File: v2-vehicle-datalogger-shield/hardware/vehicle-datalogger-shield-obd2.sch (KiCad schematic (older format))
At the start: 47 parts

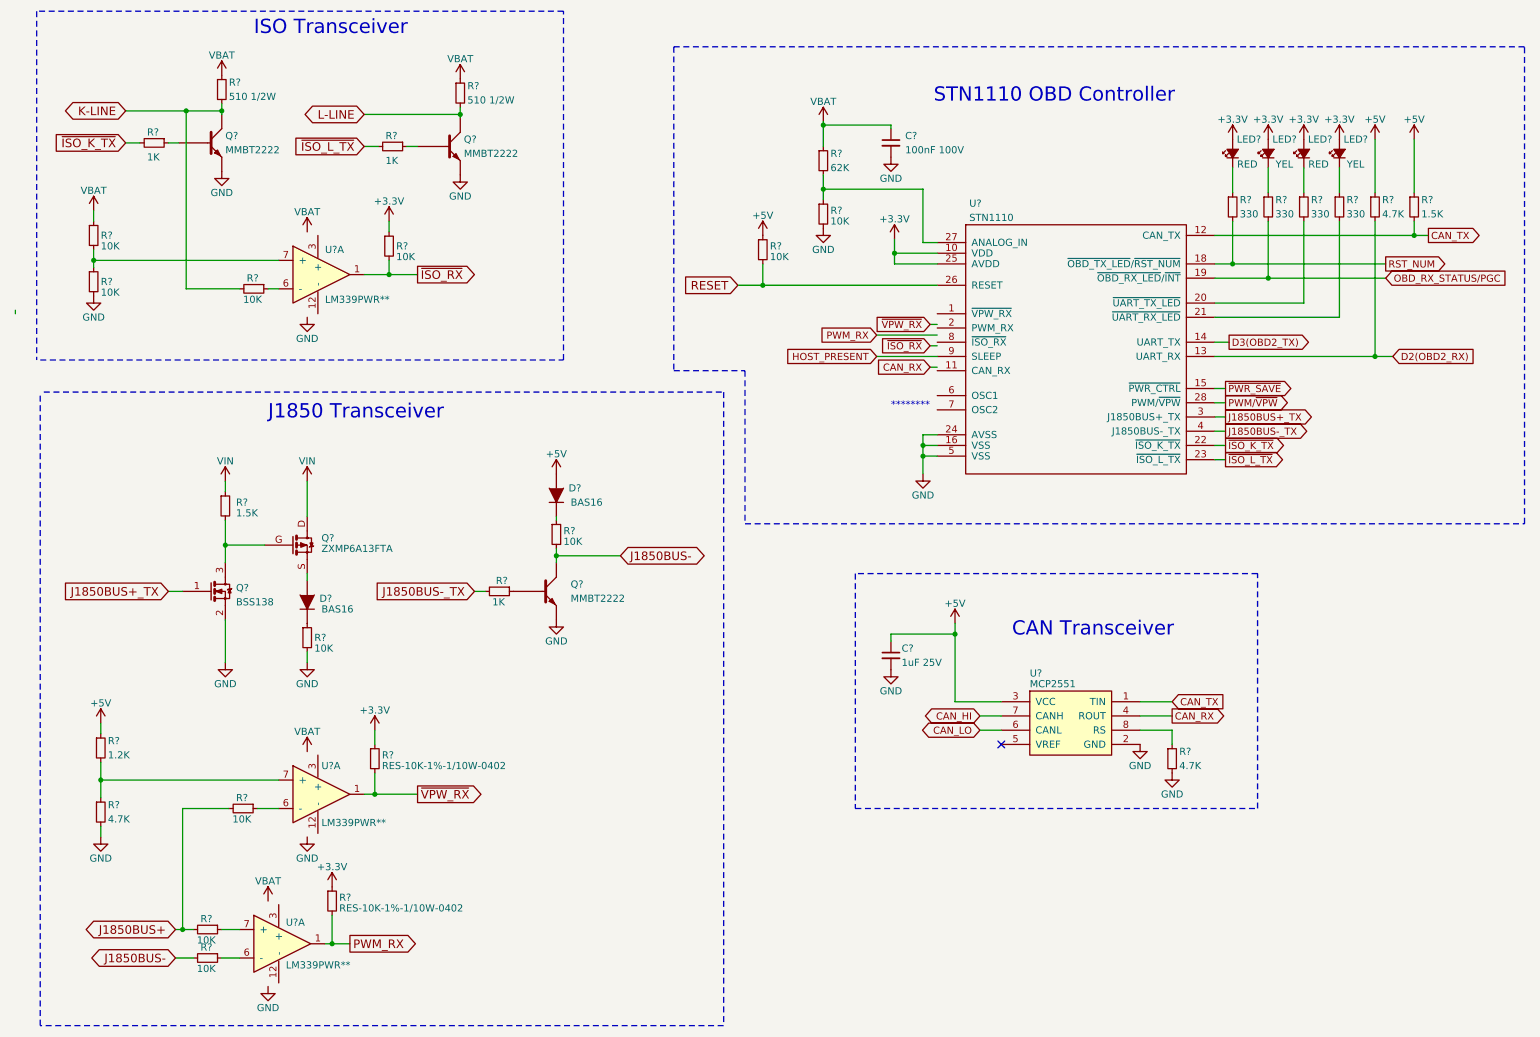
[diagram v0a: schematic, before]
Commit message: Added CC3000 and fixed all other packages. Ready for check.
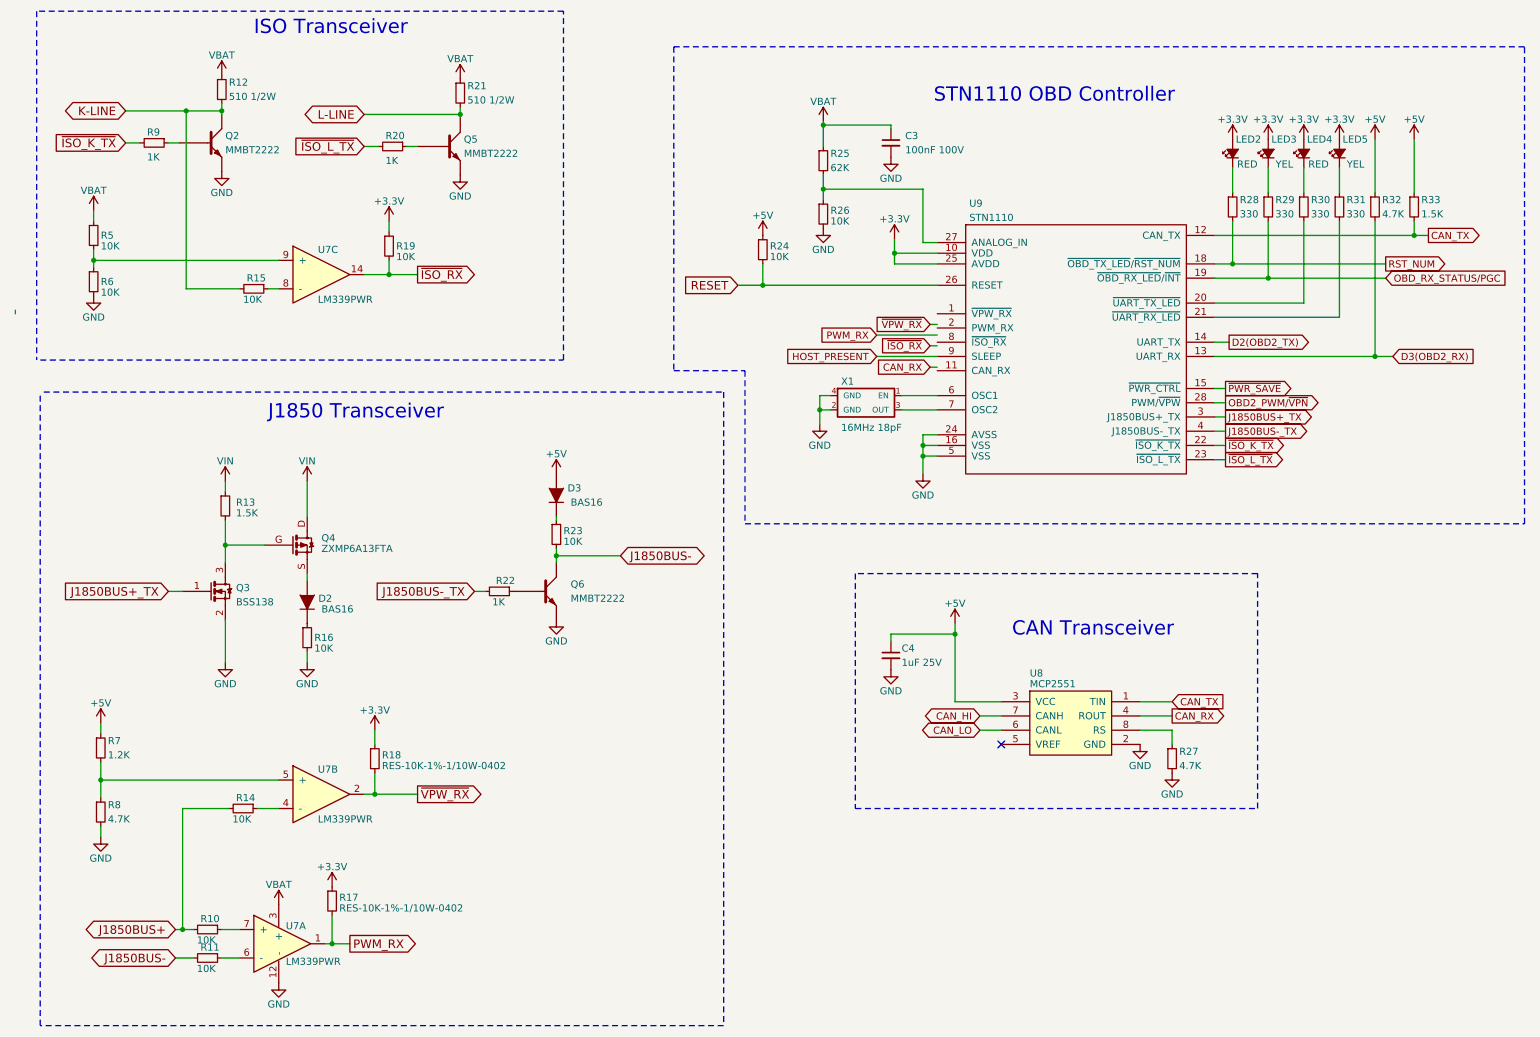
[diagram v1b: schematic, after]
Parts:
- removed U? (x3): LM339PWR**, TSSOP14, symbol IC-DIFF-COMPARE-LM339PWR-TSSOP14
- added U7: LM339PWR, TSSOP14, symbol IC-DIFF-COMPARE-LM339PWR-TSSOP14
- added X1: 16MHz 18pF, CTS-4SMD, symbol CRYSTAL-16MHZ-18PF-40OHM-CTS-4SMD
- gave numbers to parts that had none: 44
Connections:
- net labels added: D2(OBD2_TX), D3(OBD2_RX), OBD2_PWM/~VPN
- net labels removed: D2(OBD2_RX), D3(OBD2_TX), PWM/~VPW
- wire segments 102 -> 107
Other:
- note removed: "********"

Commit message: Pothole vehicle datalogger shield v1.0 schematic is done.
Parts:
- removed C4: 1uF 25V, 0603, symbol CAP-CER-1UF-25V-X7R-0603
- added W1, W2, W3: TEST_1P, Wickerlib:Pin_Header_Straight_1x01, symbol TEST_1P
- C3: value 100nF 100V -> 100nF; footprint 0603 -> Wickerlib:0603
- D2, D3: footprint SOD323 -> Wickerlib:SOD-323
- LED2, LED3, LED4, LED5: footprint 0603 -> Wickerlib:0603
- Q2, Q3, Q4, Q5, Q6: footprint SOT23-3 -> Wickerlib:SOT-23-3
- R10, R11, R13, R14, R15, R16, R17, R18, R19, R20, R22, R23, R24, R25, R26, R27, R28, R29, R30, R31, R32, R33, R5, R6, R7, R8, R9: footprint 0402 -> Wickerlib:0402
- U7: footprint TSSOP14 -> Wickerlib:UNDEFINED
- U8: renamed from U9; footprint QFN28 -> Wickerlib:QFN-32-1EP_5x5mm_Pitch0.5mm
- U9: renamed from U8; footprint SOIC8 -> Wickerlib:SOIC-8_3.9x4.9mm_Pitch1.27mm
- X1: footprint CTS-4SMD -> Wickerlib:CRYSTAL-CTS-4SMD
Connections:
- net labels added: K_LINE, L_LINE, SLEEP, ~PWR_CTRL
- net labels removed: HOST_PRESENT, K-LINE, L-LINE, ~PWR_SAVE
- wire segments 107 -> 111
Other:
- moved on the sheet: LED2, LED3, LED4, LED5, R24, R25, R26, R28, R29, R30, R31, R32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

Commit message: Added missing footprints, finished symbol-footprint association.
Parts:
- R12, R21: footprint 2010 -> Wickerlib:2010
- U7: footprint Wickerlib:UNDEFINED -> Wickerlib:TSSOP-14_4.4x5mm_Pitch0.65mm
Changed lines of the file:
@@
 F 0 "R12" H 2000 1175 50  0000 L CNN
 F 1 "510 1/2W" H 2000 1075 50  0000 L CNN
-F 2 "2010" H 1950 775 50  0001 C CIN
+F 2 "Wickerlib:2010" H 1950 775 50  0001 C CIN
 F 3 "http://rohmfs.rohm.com/en/products/databook/datasheet/passive/resistor/chip_resistor/mcr.pdf" H 1950 1125 5   0001 C CNN
 F 4 "2010" H 1950 775 50  0001 C CIN "Package"
@@
 F 0 "R21" H 3675 1200 50  0000 L CNN
 F 1 "510 1/2W" H 3675 1100 50  0000 L CNN
-F 2 "2010" H 3625 800 50  0001 C CIN
+F 2 "Wickerlib:2010" H 3625 800 50  0001 C CIN
 F 3 "http://rohmfs.rohm.com/en/products/databook/datasheet/passive/resistor/chip_resistor/mcr.pdf" H 3625 1150 5   0001 C CNN
 F 4 "2010" H 3625 800 50  0001 C CIN "Package"
@@
 F 0 "U7" H 2400 7250 50  0000 L CNN
 F 1 "LM339PWR" H 2400 7000 50  0000 L CNN
-F 2 "Wickerlib:UNDEFINED" H 2375 6775 50  0001 C CIN
+F 2 "Wickerlib:TSSOP-14_4.4x5mm_Pitch0.65mm" H 2375 6775 50  0001 C CIN
 F 3 "http://www.ti.com/lit/ds/symlink/lm139a.pdf" H 2375 7125 5   0001 C CNN
 F 4 "UNDEFINED" H 2375 6775 50  0001 C CIN "Package"
@@
 F 0 "U7" H 2625 6250 50  0000 L CNN
 F 1 "LM339PWR" H 2625 5900 50  0000 L CNN
-F 2 "Wickerlib:UNDEFINED" H 2650 5725 50  0001 C CIN
+F 2 "Wickerlib:TSSOP-14_4.4x5mm_Pitch0.65mm" H 2650 5725 50  0001 C CIN
 F 3 "http://www.ti.com/lit/ds/symlink/lm139a.pdf" H 2650 6075 5   0001 C CNN
 F 4 "UNDEFINED" H 2650 5725 50  0001 C CIN "Package"
@@
 F 0 "U7" H 2625 2600 50  0000 L CNN
 F 1 "LM339PWR" H 2625 2250 50  0000 L CNN
-F 2 "Wickerlib:UNDEFINED" H 2650 2075 50  0001 C CIN
+F 2 "Wickerlib:TSSOP-14_4.4x5mm_Pitch0.65mm" H 2650 2075 50  0001 C CIN
 F 3 "http://www.ti.com/lit/ds/symlink/lm139a.pdf" H 2650 2425 5   0001 C CNN
 F 4 "UNDEFINED" H 2650 2075 50  0001 C CIN "Package"

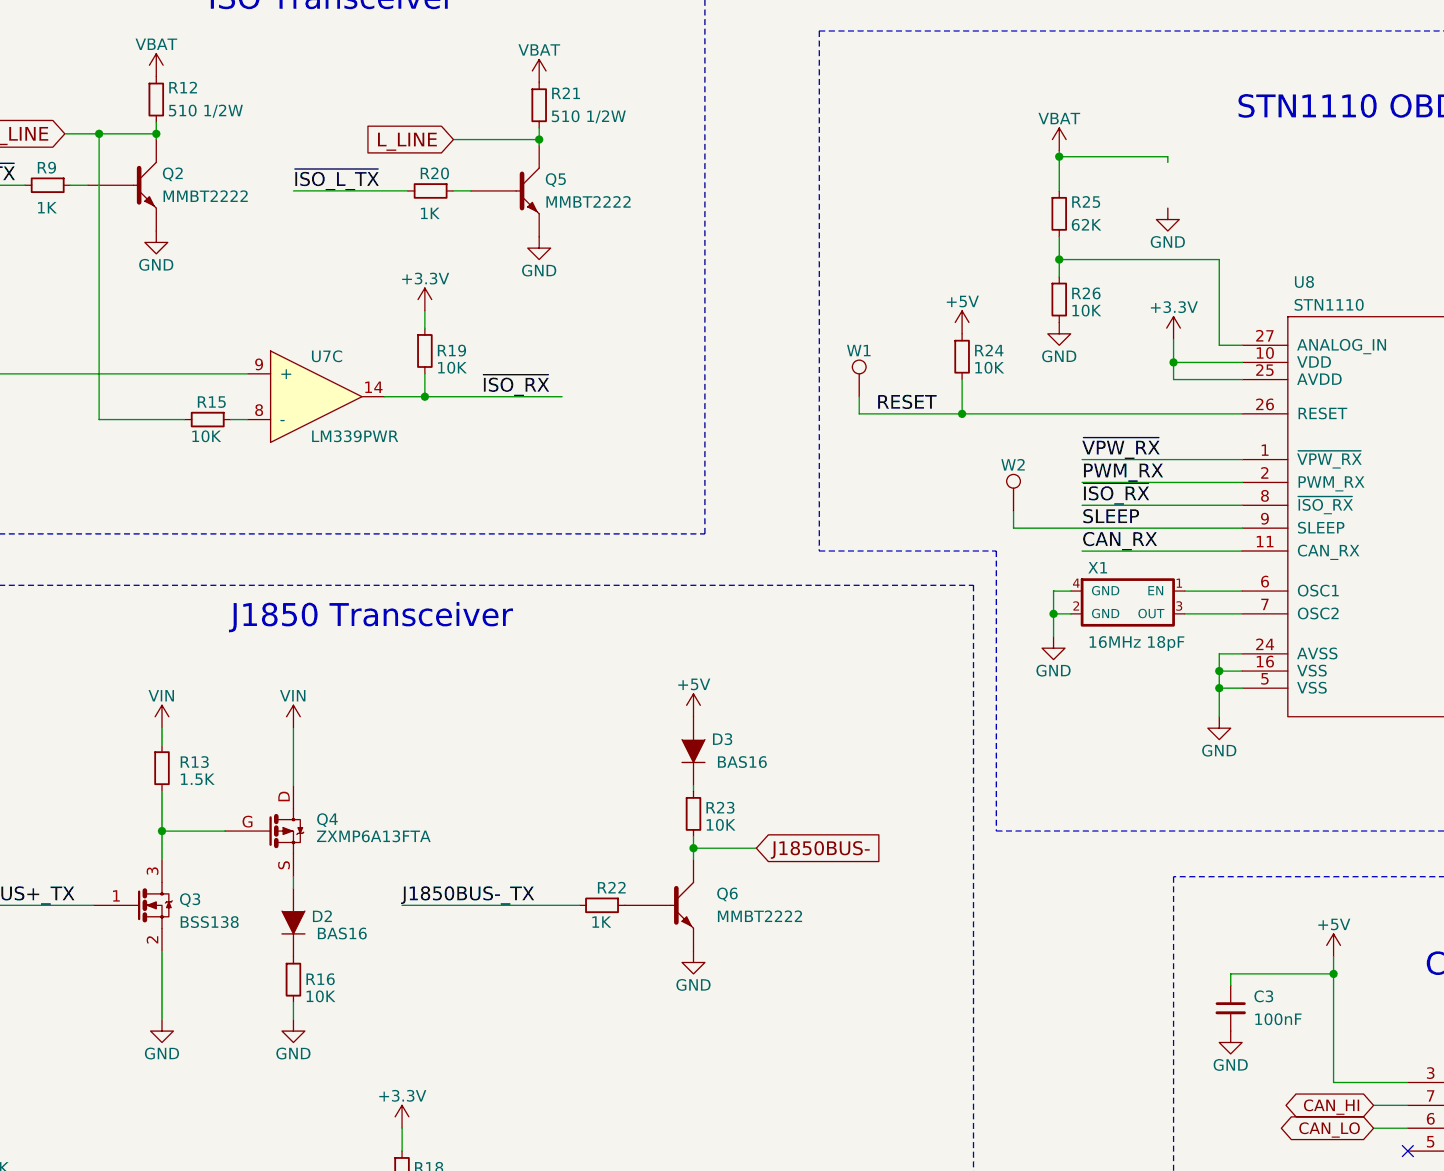
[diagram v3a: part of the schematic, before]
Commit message: Updated schematic, BOM, and spread out footprints. Ready to layout.
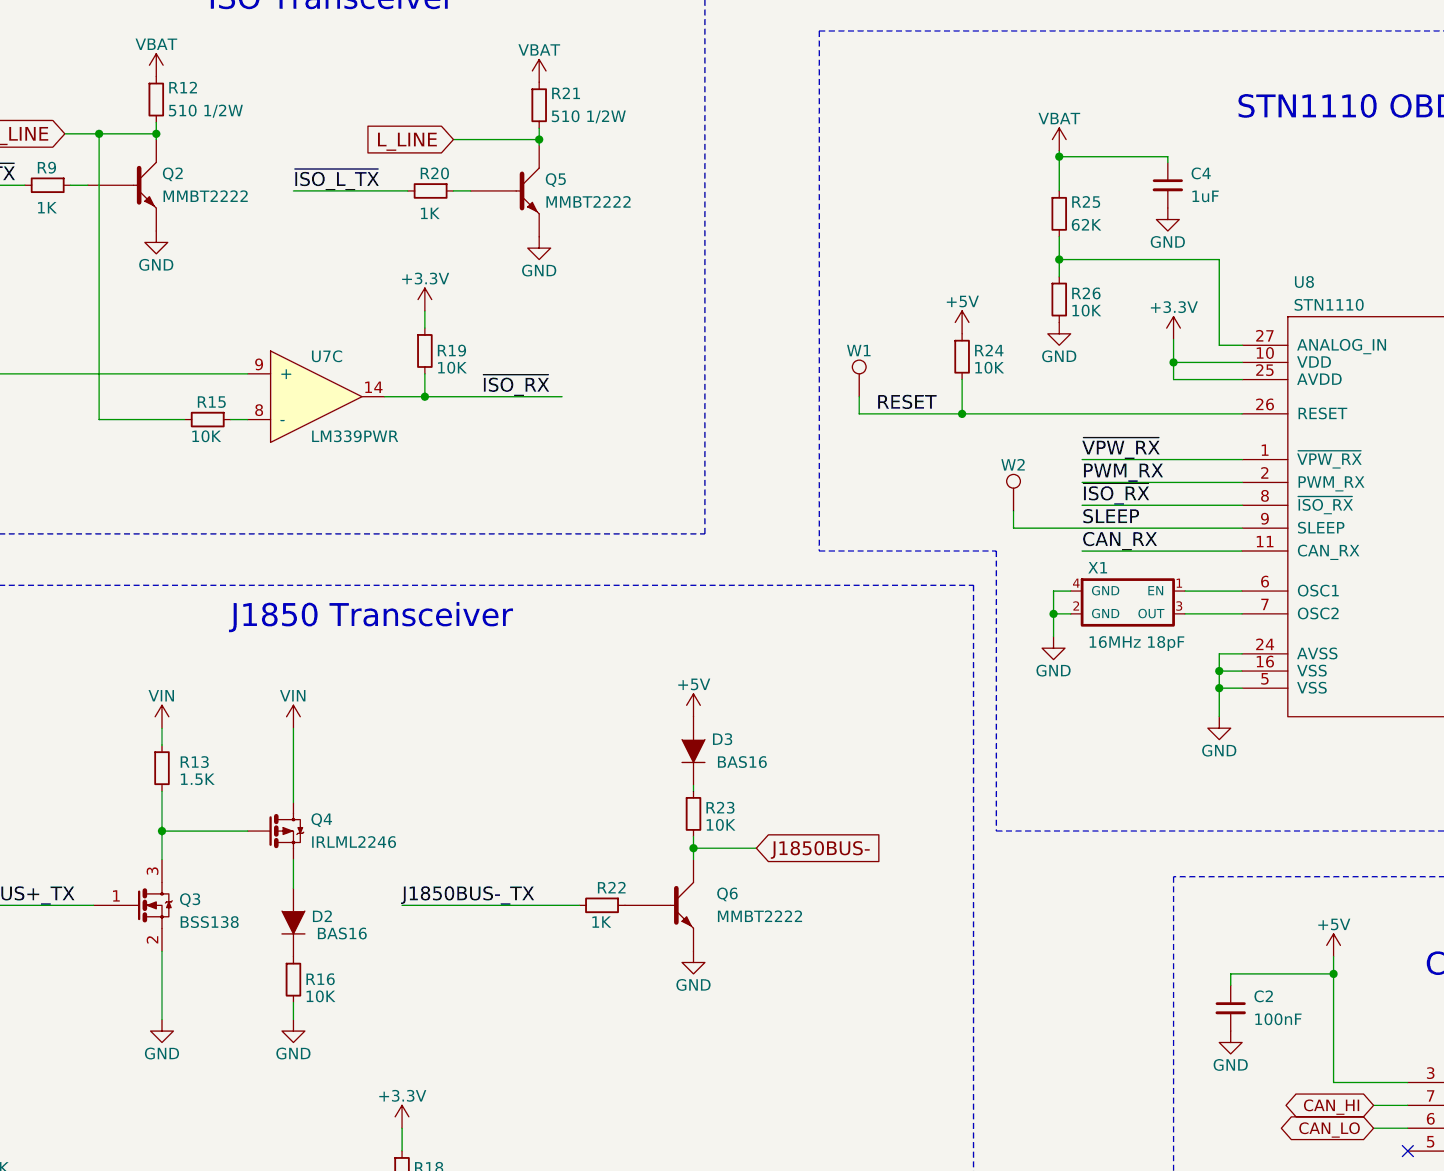
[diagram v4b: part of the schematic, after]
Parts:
- removed Q4: ZXMP6A13FTA, Wickerlib:SOT-23-3, symbol ZXMP6A13FTA
- added C4: 1uF, Wickerlib:0805, symbol CAP-CER-1UF-25V-X7R-0805
- added Q4: IRLML2246, Wickerlib:SOT-23-3, symbol MOSFET-P-20V-2.6A-IRLML2246
- renumbered C3 to C2
